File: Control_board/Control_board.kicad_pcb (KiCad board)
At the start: 4 copper layers, 123.8 x 99.7 mm, 26 parts, among them J1 ICSP, J2 Conn_02x32_Odd_Even, J3 Conn_02x32_Odd_Even, SW1 SW_Push, SW2 SW_Push, U1 74LS74, U10 27C512, U11 ATtiny85-20P, U2 74LS74, U3 74LS273, U4 74LS373, U5 74LS192, U6 74LS373, U7 27C512, U8 27C512, U9 27C512

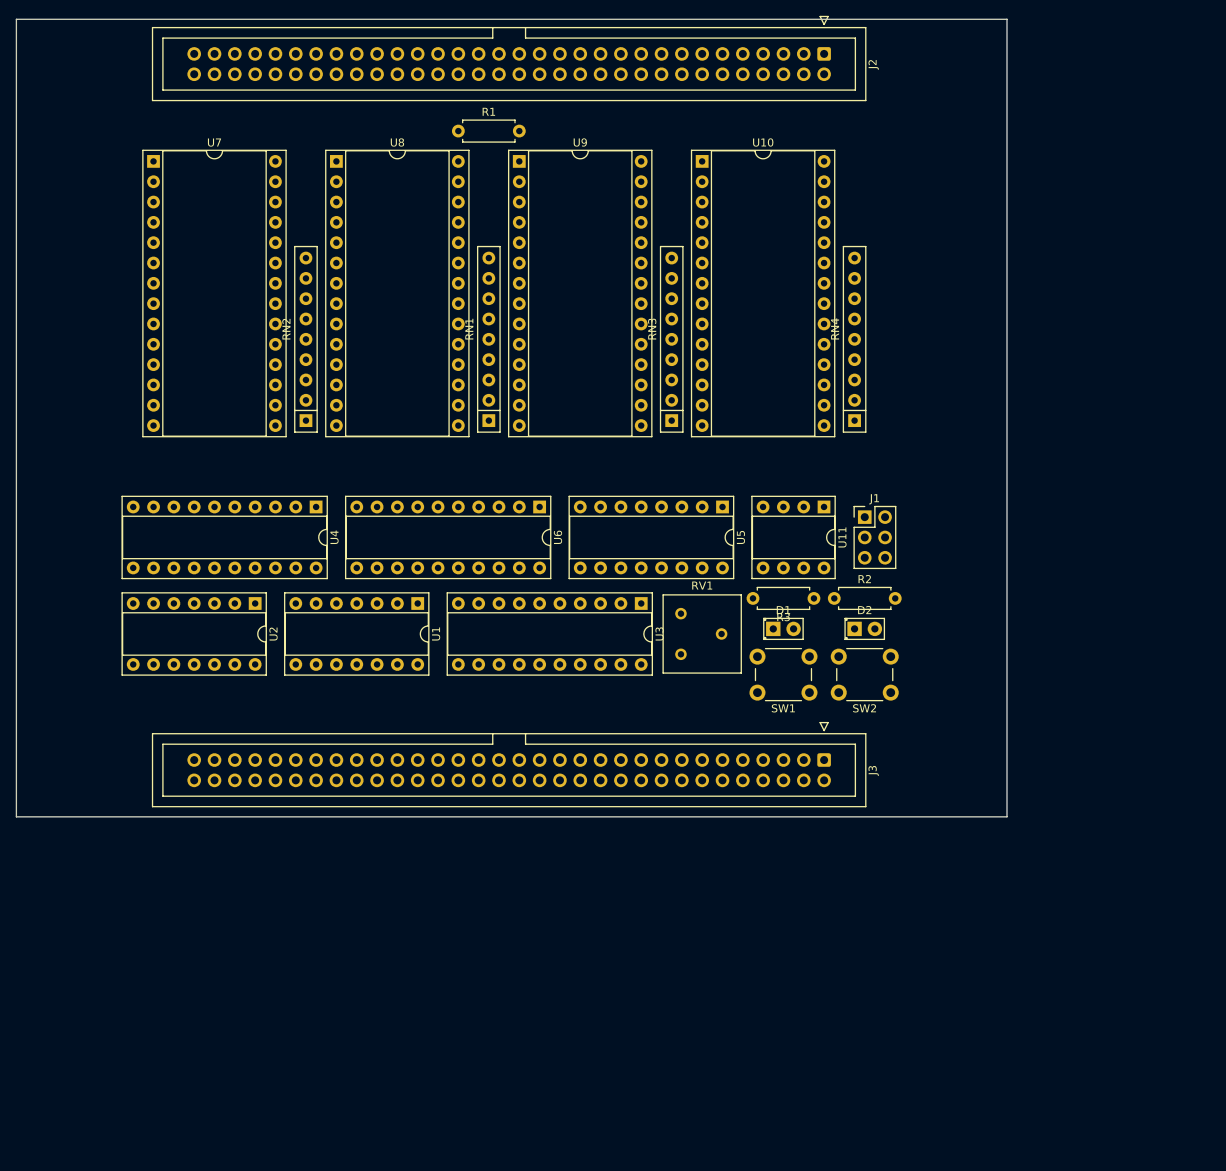
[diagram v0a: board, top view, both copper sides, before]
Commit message: Control board ready for routing
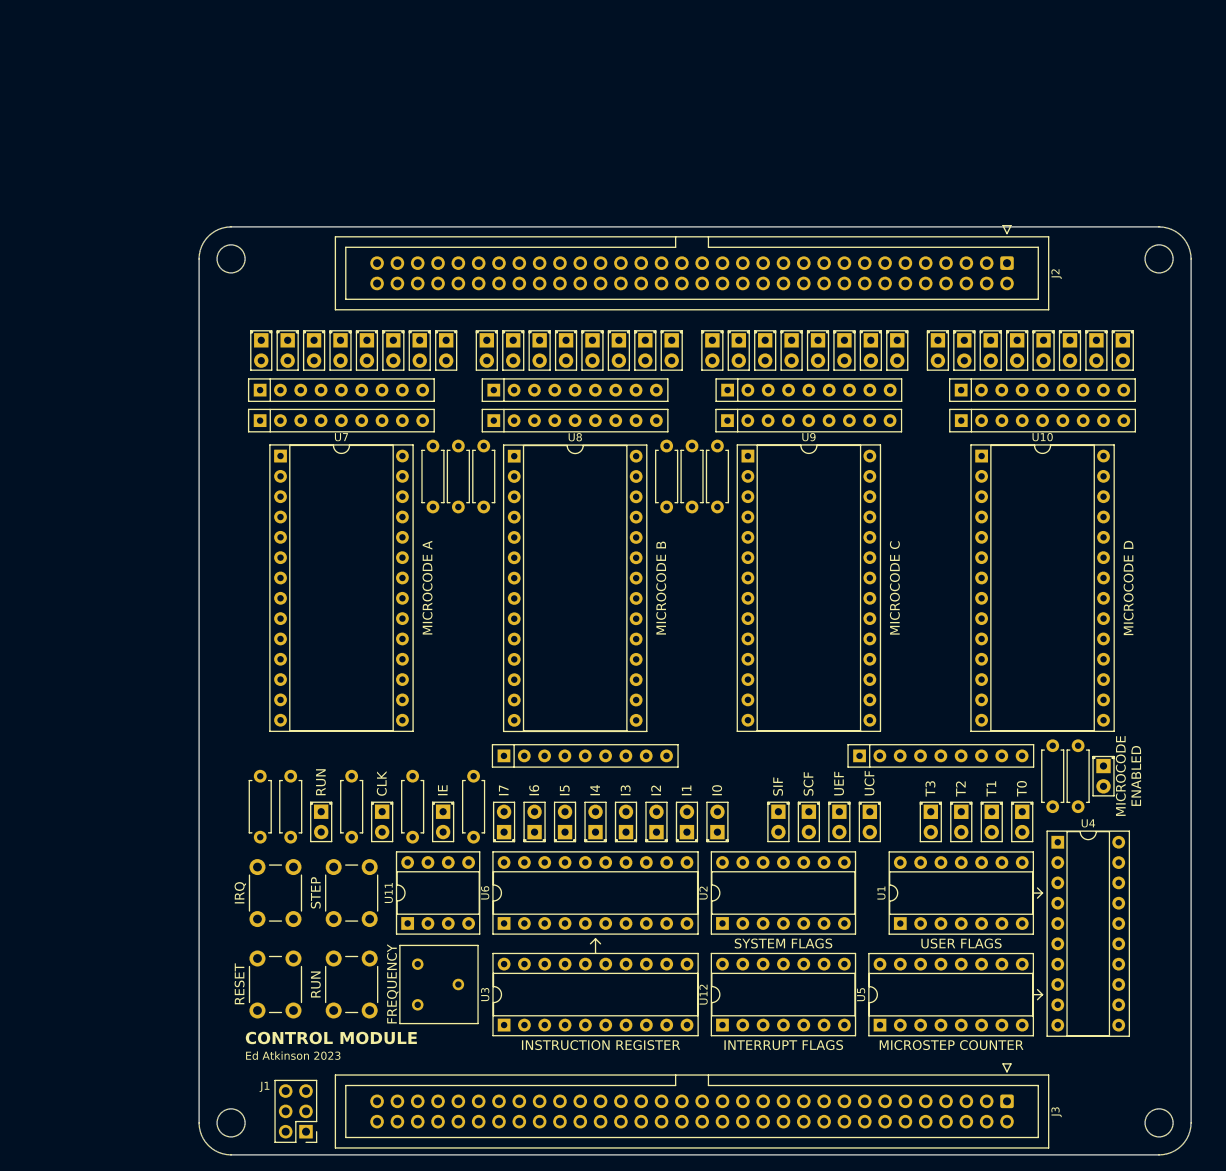
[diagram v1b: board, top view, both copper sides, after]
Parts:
- added D10: LED, LED_THT:LED_D2.0mm_W4.8mm_H2.5mm_FlatTop, F.Cu at (149.2, 118.1)
- added D11: LED, LED_THT:LED_D2.0mm_W4.8mm_H2.5mm_FlatTop, F.Cu at (145.4, 118.1)
- added D12: LED, LED_THT:LED_D2.0mm_W4.8mm_H2.5mm_FlatTop, F.Cu at (137.8, 120.7)
- added D13: LED, LED_THT:LED_D2.0mm_W4.8mm_H2.5mm_FlatTop, F.Cu at (134.0, 120.7)
- added D14: LED, LED_THT:LED_D2.0mm_W4.8mm_H2.5mm_FlatTop, F.Cu at (130.2, 120.7)
- added D15: LED, LED_THT:LED_D2.0mm_W4.8mm_H2.5mm_FlatTop, F.Cu at (126.4, 120.7)
- added D16: LED, LED_THT:LED_D2.0mm_W4.8mm_H2.5mm_FlatTop, F.Cu at (122.6, 120.7)
- added D17: LED, LED_THT:LED_D2.0mm_W4.8mm_H2.5mm_FlatTop, F.Cu at (118.7, 120.7)
- added D18: LED, LED_THT:LED_D2.0mm_W4.8mm_H2.5mm_FlatTop, F.Cu at (114.9, 120.7)
- added D19: LED, LED_THT:LED_D2.0mm_W4.8mm_H2.5mm_FlatTop, F.Cu at (111.1, 120.7)
- added D20: LED, LED_THT:LED_D2.0mm_W4.8mm_H2.5mm_FlatTop, F.Cu at (125.5, 59.2)
- added D21: LED, LED_THT:LED_D2.0mm_W4.8mm_H2.5mm_FlatTop, F.Cu at (122.2, 59.2)
- added D22: LED, LED_THT:LED_D2.0mm_W4.8mm_H2.5mm_FlatTop, F.Cu at (115.6, 59.2)
- added D23: LED, LED_THT:LED_D2.0mm_W4.8mm_H2.5mm_FlatTop, F.Cu at (109.0, 59.2)
- added D24: LED, LED_THT:LED_D2.0mm_W4.8mm_H2.5mm_FlatTop, F.Cu at (112.3, 59.2)
- added D25: LED, LED_THT:LED_D2.0mm_W4.8mm_H2.5mm_FlatTop, F.Cu at (118.9, 59.2)
- added D26: LED, LED_THT:LED_D2.0mm_W4.8mm_H2.5mm_FlatTop, F.Cu at (128.8, 59.2)
- added D27: LED, LED_THT:LED_D2.0mm_W4.8mm_H2.5mm_FlatTop, F.Cu at (132.1, 59.2)
- added D28: LED, LED_THT:LED_D2.0mm_W4.8mm_H2.5mm_FlatTop, F.Cu at (80.8, 59.2)
- added D29: LED, LED_THT:LED_D2.0mm_W4.8mm_H2.5mm_FlatTop, F.Cu at (84.1, 59.2)
- added D3: LED, LED_THT:LED_D2.0mm_W4.8mm_H2.5mm_FlatTop, F.Cu at (175.9, 118.1)
- added D30: LED, LED_THT:LED_D2.0mm_W4.8mm_H2.5mm_FlatTop, F.Cu at (87.4, 59.2)
- added D31: LED, LED_THT:LED_D2.0mm_W4.8mm_H2.5mm_FlatTop, F.Cu at (90.7, 59.2)
- added D32: LED, LED_THT:LED_D2.0mm_W4.8mm_H2.5mm_FlatTop, F.Cu at (94.0, 59.2)
- added D33: LED, LED_THT:LED_D2.0mm_W4.8mm_H2.5mm_FlatTop, F.Cu at (97.3, 59.2)
- added D34: LED, LED_THT:LED_D2.0mm_W4.8mm_H2.5mm_FlatTop, F.Cu at (100.6, 59.2)
- added D35: LED, LED_THT:LED_D2.0mm_W4.8mm_H2.5mm_FlatTop, F.Cu at (103.9, 59.2)
- added D36: LED, LED_THT:LED_D2.0mm_W4.8mm_H2.5mm_FlatTop, F.Cu at (160.3, 59.2)
- added D37: LED, LED_THT:LED_D2.0mm_W4.8mm_H2.5mm_FlatTop, F.Cu at (157.0, 59.2)
- added D38: LED, LED_THT:LED_D2.0mm_W4.8mm_H2.5mm_FlatTop, F.Cu at (153.7, 59.2)
- added D39: LED, LED_THT:LED_D2.0mm_W4.8mm_H2.5mm_FlatTop, F.Cu at (150.4, 59.2)
- added D4: LED, LED_THT:LED_D2.0mm_W4.8mm_H2.5mm_FlatTop, F.Cu at (172.1, 118.1)
- added D40: LED, LED_THT:LED_D2.0mm_W4.8mm_H2.5mm_FlatTop, F.Cu at (147.1, 59.2)
- added D41: LED, LED_THT:LED_D2.0mm_W4.8mm_H2.5mm_FlatTop, F.Cu at (143.8, 59.2)
- added D42: LED, LED_THT:LED_D2.0mm_W4.8mm_H2.5mm_FlatTop, F.Cu at (140.5, 59.2)
- added D43: LED, LED_THT:LED_D2.0mm_W4.8mm_H2.5mm_FlatTop, F.Cu at (137.2, 59.2)
- added D44: LED, LED_THT:LED_D2.0mm_W4.8mm_H2.5mm_FlatTop, F.Cu at (165.4, 59.2)
- added D45: LED, LED_THT:LED_D2.0mm_W4.8mm_H2.5mm_FlatTop, F.Cu at (185.2, 59.2)
- added D46: LED, LED_THT:LED_D2.0mm_W4.8mm_H2.5mm_FlatTop, F.Cu at (181.9, 59.2)
- added D47: LED, LED_THT:LED_D2.0mm_W4.8mm_H2.5mm_FlatTop, F.Cu at (178.6, 59.2)
- added D48: LED, LED_THT:LED_D2.0mm_W4.8mm_H2.5mm_FlatTop, F.Cu at (175.3, 59.2)
- added D49: LED, LED_THT:LED_D2.0mm_W4.8mm_H2.5mm_FlatTop, F.Cu at (172.0, 59.2)
- added D5: LED, LED_THT:LED_D2.0mm_W4.8mm_H2.5mm_FlatTop, F.Cu at (168.3, 118.1)
- added D50: LED, LED_THT:LED_D2.0mm_W4.8mm_H2.5mm_FlatTop, F.Cu at (168.7, 59.2)
- added D51: LED, LED_THT:LED_D2.0mm_W4.8mm_H2.5mm_FlatTop, F.Cu at (188.5, 59.2)
- added D52: LED, LED_THT:LED_D2.0mm_W4.8mm_H2.5mm_FlatTop, F.Cu at (186.1, 112.4)
- added D6: LED, LED_THT:LED_D2.0mm_W4.8mm_H2.5mm_FlatTop, F.Cu at (103.5, 118.1)
- added D7: LED, LED_THT:LED_D2.0mm_W4.8mm_H2.5mm_FlatTop, F.Cu at (164.5, 118.1)
- added D8: LED, LED_THT:LED_D2.0mm_W4.8mm_H2.5mm_FlatTop, F.Cu at (156.8, 118.1)
- added D9: LED, LED_THT:LED_D2.0mm_W4.8mm_H2.5mm_FlatTop, F.Cu at (153.0, 118.1)
- added H1: MountingHole, MountingHole:MountingHole_3.5mm, F.Cu at (77.0, 49.0)
- added H2: MountingHole, MountingHole:MountingHole_3.5mm, F.Cu at (193.0, 49.0)
- added H3: MountingHole, MountingHole:MountingHole_3.5mm, F.Cu at (77.0, 157.0)
- added H4: MountingHole, MountingHole:MountingHole_3.5mm, F.Cu at (193.0, 157.0)
- added R10: 1K, Resistor_THT:R_Axial_DIN0207_L6.3mm_D2.5mm_P7.62mm_Horizontal, F.Cu at (80.6, 113.7)
- added R11: 1K, Resistor_THT:R_Axial_DIN0207_L6.3mm_D2.5mm_P7.62mm_Horizontal, F.Cu at (179.7, 109.9)
- added R12: 330R, Resistor_THT:R_Axial_DIN0207_L6.3mm_D2.5mm_P7.62mm_Horizontal, F.Cu at (182.9, 109.9)
- added R13: 1K, Resistor_THT:R_Axial_DIN0207_L6.3mm_D2.5mm_P7.62mm_Horizontal, F.Cu at (84.5, 113.7)
- added R4: 330R, Resistor_THT:R_Axial_DIN0207_L6.3mm_D2.5mm_P7.62mm_Horizontal, F.Cu at (107.3, 113.7)
- added R5: 1K, Resistor_THT:R_Axial_DIN0207_L6.3mm_D2.5mm_P7.62mm_Horizontal, F.Cu at (137.8, 80.0)
- added R6: 1K, Resistor_THT:R_Axial_DIN0207_L6.3mm_D2.5mm_P7.62mm_Horizontal, F.Cu at (134.6, 80.0)
- added R7: 330R, Resistor_THT:R_Axial_DIN0207_L6.3mm_D2.5mm_P7.62mm_Horizontal, F.Cu at (108.6, 80.0)
- added R8: 330R, Resistor_THT:R_Axial_DIN0207_L6.3mm_D2.5mm_P7.62mm_Horizontal, F.Cu at (105.4, 80.0)
- added R9: 330R, Resistor_THT:R_Axial_DIN0207_L6.3mm_D2.5mm_P7.62mm_Horizontal, F.Cu at (102.2, 80.0)
- added RN10: 330R, Resistor_THT:R_Array_SIP9, F.Cu at (168.3, 65.4)
- added RN5: 330R, Resistor_THT:R_Array_SIP9, F.Cu at (155.6, 111.1)
- added RN6: 330R, Resistor_THT:R_Array_SIP9, F.Cu at (111.1, 111.1)
- added RN7: 330R, Resistor_THT:R_Array_SIP9, F.Cu at (109.8, 65.4)
- added RN8: 330R, Resistor_THT:R_Array_SIP9, F.Cu at (80.6, 65.4)
- added RN9: 330R, Resistor_THT:R_Array_SIP9, F.Cu at (139.1, 65.4)
- added SW3: SW_Push, Button_Switch_THT:SW_PUSH_6mm, F.Cu at (80.3, 142.9)
- added SW4: SW_Push, Button_Switch_THT:SW_PUSH_6mm, F.Cu at (80.3, 131.5)
- added U12: 74LS74, Package_DIP:DIP-14_W7.62mm_Socket, F.Cu at (138.4, 144.8)
- RN1, RN2, RN3, RN4: value R_Network08 -> 1K
- moved J1 103.8 mm to (86.4, 158.1), turned to 180 degrees
- moved U4 101.7 mm to (180.3, 121.9), turned to 0 degrees
- moved U11 73.6 mm to (99.1, 132.1), turned to 90 degrees
- moved U1 72.4 mm to (160.7, 132.1), turned to 90 degrees
- moved U2 70.8 mm to (138.4, 132.1), turned to 90 degrees
- moved SW2 68.7 mm to (94.3, 125.0), turned to -90 degrees
- moved U5 67.7 mm to (158.1, 144.8), turned to 90 degrees
- moved R2 64.3 mm to (92.1, 113.7), turned to -90 degrees
- moved SW1 64.2 mm to (94.3, 136.4), turned to -90 degrees
- moved D2 63.3 mm to (95.9, 118.1), turned to -90 degrees
- moved D1 61.0 mm to (88.3, 118.1), turned to -90 degrees
- moved U3 55.4 mm to (111.1, 144.8), turned to 90 degrees
- moved R3 54.9 mm to (99.7, 113.7), turned to -90 degrees
- moved RV1 54.8 mm to (100.3, 142.2)
- moved R1 53.7 mm to (131.4, 80.0), turned to 90 degrees
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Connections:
- J2 pad 13: /INTERRUPT_FLAG -> /~{INTERRUPT_FLAG}
- J3 pad 13: /INTERRUPT_FLAG -> /~{INTERRUPT_FLAG}
- RN1 pad 5: unconnected-(RN1-R4-Pad5) -> /COUNTER_RESET
- RN1 pad 6: /COUNTER_RESET -> unconnected-(RN1-R5-Pad6)
- RN1 pad 7: /INTERRUPT_UPDATE -> unconnected-(RN1-R6-Pad7)
- U1 pad 1: unconnected-(U1A-~{R}-Pad1) -> +5V
- U1 pad 10: unconnected-(U1B-~{S}-Pad10) -> +5V
- U1 pad 13: unconnected-(U1B-~{R}-Pad13) -> +5V
- U1 pad 4: unconnected-(U1A-~{S}-Pad4) -> +5V
- U2 pad 1: unconnected-(U2A-~{R}-Pad1) -> +5V
- U2 pad 10: unconnected-(U2B-~{S}-Pad10) -> +5V
- U2 pad 11: /INTERRUPT_UPDATE -> GND
- U2 pad 12: /INTERRUPT_FLAG -> GND
- U2 pad 13: /~{RESET} -> +5V
- U2 pad 4: unconnected-(U2A-~{S}-Pad4) -> +5V
- U2 pad 9: Net-(U2B-Q) -> unconnected-(U2B-Q-Pad9)
- U4 pad 12: unconnected-(U4-O4-Pad12) -> /MA4
- U4 pad 13: GND -> Net-(U1A-Q)
- U4 pad 14: GND -> Net-(U1B-Q)
- U4 pad 15: unconnected-(U4-O5-Pad15) -> /MA5
- U4 pad 16: unconnected-(U4-O6-Pad16) -> /MA6
- U4 pad 17: GND -> Net-(U2A-Q)
- U4 pad 18: GND -> Net-(U12A-Q)
- U4 pad 19: unconnected-(U4-O7-Pad19) -> /MA7
- U4 pad 2: /MA12 -> /MA0
- U4 pad 3: Net-(U1A-Q) -> Net-(U4-D0)
- U4 pad 4: Net-(U1B-Q) -> Net-(U4-D1)
- U4 pad 5: /MA13 -> /MA1
- U4 pad 6: /MA14 -> /MA2
- U4 pad 7: Net-(U2A-Q) -> Net-(U4-D2)
- U4 pad 8: Net-(U2B-Q) -> Net-(U4-D3)
- U4 pad 9: /MA15 -> /MA3
- U5 pad 2: /MA1 -> Net-(U4-D1)
- U5 pad 3: /MA0 -> Net-(U4-D0)
- U5 pad 6: /MA2 -> Net-(U4-D2)
- U5 pad 7: /MA3 -> Net-(U4-D3)
- U6 pad 12: /MA8 -> /MA12
- U6 pad 15: /MA9 -> /MA13
- U6 pad 16: /MA10 -> /MA14
- U6 pad 19: /MA11 -> /MA15
- U6 pad 2: /MA4 -> /MA8
- U6 pad 5: /MA5 -> /MA9
- U6 pad 6: /MA6 -> /MA10
- U6 pad 9: /MA7 -> /MA11
- U8 pad 15: unconnected-(U8-D3-Pad15) -> /COUNTER_RESET
- U8 pad 16: /COUNTER_RESET -> /~{INTERRUPT_ENABLE}
- U8 pad 17: /INTERRUPT_UPDATE -> /~{INTERRUPT_DISABLE}
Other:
- board size 123.8 x 99.7 mm -> 124 x 116 mm
- board text added: "CLK"
- board text added: "CONTROL MODULE"
- board text added: "Ed Atkinson 2023"
- board text added: "FREQUENCY"
- board text added: "I0"
- board text added: "I1"
- board text added: "I2"
- board text added: "I3"
- board text added: "I4"
- board text added: "I5"
- board text added: "I6"
- board text added: "I7"
- board text added: "IE"
- board text added: "INSTRUCTION REGISTER"
- board text added: "INTERRUPT FLAGS"
- board text added: "IRQ"
- board text added: "MICROCODE A"
- board text added: "MICROCODE B"
- board text added: "MICROCODE C"
- board text added: "MICROCODE D"
- board text added: "MICROCODE ENABLED"
- board text added: "MICROSTEP COUNTER"
- board text added: "RESET"
- board text added: "RUN"
- board text added: "SCF"
- board text added: "SIF"
- board text added: "STEP"
- board text added: "SYSTEM FLAGS"
- board text added: "T0"
- board text added: "T1"
- board text added: "T2"
- board text added: "T3"
- board text added: "UCF"
- board text added: "UEF"
- board text added: "USER FLAGS"

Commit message: Control board and connector bridge ready for ordering
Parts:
- J3: value Conn_02x32_Odd_Even -> Conn_01x02; footprint Connector_IDC:IDC-Header_2x32_P2.54mm_Vertical -> Connector_PinHeader_2.54mm:PinHeader_1x02_P2.54mm_Vertical
- moved R9 63.5 mm to (163.8, 64.8), turned to -90 degrees
- moved R6 59.7 mm to (194.3, 82.5)
- moved R1 59.1 mm to (190.5, 82.5)
- moved RN7 58.4 mm to (168.3, 65.4)
- moved RN1 58.4 mm to (168.3, 69.2)
- moved RN3 58.4 mm to (80.6, 69.2)
- moved R7 57.4 mm to (165.7, 74.9), turned to -90 degrees
- moved R8 56.7 mm to (161.9, 74.9), turned to -90 degrees
- moved D23 56.4 mm to (165.4, 59.2)
- moved D20 56.4 mm to (181.9, 59.2)
- moved D21 56.4 mm to (178.6, 59.2)
- moved D22 56.4 mm to (172.0, 59.2)
- moved D24 56.4 mm to (168.7, 59.2)
- moved D26 56.4 mm to (185.2, 59.2)
- moved D25 56.4 mm to (175.3, 59.2)
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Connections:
- D20 pad 1: /~{INTERRUPT_DISABLE} -> /IR_LOAD
- D21 pad 1: /~{INTERRUPT_ENABLE} -> /INT_EN_TOGGLE
- D28 pad 1: Net-(D28-K) -> /~{SP_OUT}
- D28 pad 2: /PC_H_LOAD -> Net-(D28-A)
- D29 pad 1: Net-(D29-K) -> /~{ALU_OUT}
- D29 pad 2: /PC_L_LOAD -> Net-(D29-A)
- D30 pad 1: Net-(D30-K) -> /~{PC_OUT}
- D30 pad 2: /SP_H_LOAD -> Net-(D30-A)
- D31 pad 1: Net-(D31-K) -> /~{A_OUT}
- D31 pad 2: /SP_L_LOAD -> Net-(D31-A)
- D32 pad 1: Net-(D32-K) -> /~{T_OUT}
- D32 pad 2: /B_LOAD -> Net-(D32-A)
- D33 pad 1: Net-(D33-K) -> /~{BC_OUT}
- D33 pad 2: /C_LOAD -> Net-(D33-A)
- D34 pad 1: Net-(D34-K) -> /~{DE_OUT}
- D34 pad 2: /D_LOAD -> Net-(D34-A)
- D35 pad 1: Net-(D35-K) -> /~{RAM_OUT}
- D35 pad 2: /E_LOAD -> Net-(D35-A)
- D36 pad 1: /~{PC_OUT} -> Net-(D36-K)
- D36 pad 2: Net-(D36-A) -> /PC_H_LOAD
- D37 pad 1: /~{SP_OUT} -> Net-(D37-K)
- D37 pad 2: Net-(D37-A) -> /SP_H_LOAD
- D38 pad 1: /~{BC_OUT} -> Net-(D38-K)
- D38 pad 2: Net-(D38-A) -> /B_LOAD
- D39 pad 1: /~{DE_OUT} -> Net-(D39-K)
- D39 pad 2: Net-(D39-A) -> /PC_L_LOAD
- D40 pad 1: /~{A_OUT} -> Net-(D40-K)
- D40 pad 2: Net-(D40-A) -> /C_LOAD
- D41 pad 1: /~{T_OUT} -> Net-(D41-K)
- D41 pad 2: Net-(D41-A) -> /SP_L_LOAD
- D42 pad 1: /~{ALU_OUT} -> Net-(D42-K)
- D42 pad 2: Net-(D42-A) -> /E_LOAD
- D43 pad 1: /~{RAM_OUT} -> Net-(D43-K)
- D43 pad 2: Net-(D43-A) -> /D_LOAD
- D44 pad 1: /~{ADR_L_OUT} -> /~{ADR_H_OUT}
- D45 pad 1: /~{ADR_H_OUT} -> /ALU_M
- D46 pad 1: /ALU_M -> /~{ADR_L_OUT}
- D47 pad 1: /ALU_S0 -> /~{ALU_CIN}
- D48 pad 1: /ALU_S1 -> /ALU_S0
- D49 pad 1: /ALU_S2 -> /ALU_S1
- D50 pad 1: /ALU_S3 -> /ALU_S2
- D51 pad 1: /~{ALU_CIN} -> /ALU_S3
- R1 pad 2: /~{RAM_LOAD} -> /IR_LOAD
- R5 pad 2: /~{INTERRUPT_DISABLE} -> /INT_EN_TOGGLE
- R6 pad 2: /~{INTERRUPT_ENABLE} -> /~{RAM_LOAD}
- RN10 pad 2: Net-(D51-A) -> Net-(D44-A)
- RN10 pad 3: Net-(D50-A) -> Net-(D45-A)
- RN10 pad 4: Net-(D49-A) -> Net-(D46-A)
- RN10 pad 5: Net-(D48-A) -> Net-(D47-A)
- RN10 pad 6: Net-(D47-A) -> Net-(D48-A)
- RN10 pad 7: Net-(D46-A) -> Net-(D49-A)
- RN10 pad 8: Net-(D45-A) -> Net-(D50-A)
- RN10 pad 9: Net-(D44-A) -> Net-(D51-A)
- RN2 pad 3: /PC_L_LOAD -> /SP_H_LOAD
- RN2 pad 4: /SP_H_LOAD -> /B_LOAD
- RN2 pad 5: /SP_L_LOAD -> /PC_L_LOAD
- RN2 pad 6: /B_LOAD -> /C_LOAD
- RN2 pad 7: /C_LOAD -> /SP_L_LOAD
- RN2 pad 8: /D_LOAD -> /E_LOAD
- RN2 pad 9: /E_LOAD -> /D_LOAD
- RN3 pad 2: /~{RAM_OUT} -> /~{SP_OUT}
- RN3 pad 4: /~{T_OUT} -> /~{PC_OUT}
- RN3 pad 6: /~{DE_OUT} -> /~{T_OUT}
- RN3 pad 8: /~{SP_OUT} -> /~{DE_OUT}
- RN3 pad 9: /~{PC_OUT} -> /~{RAM_OUT}
- RN4 pad 2: /~{ALU_CIN} -> /~{ADR_H_OUT}
- RN4 pad 3: /ALU_S3 -> /ALU_M
- RN4 pad 4: /ALU_S2 -> /~{ADR_L_OUT}
- RN4 pad 5: /ALU_S1 -> /~{ALU_CIN}
- RN4 pad 7: /ALU_M -> /ALU_S1
- RN4 pad 8: /~{ADR_H_OUT} -> /ALU_S2
- RN4 pad 9: /~{ADR_L_OUT} -> /ALU_S3
- RN8 pad 1: GND -> +5V
- RN8 pad 2: Net-(D28-K) -> Net-(D28-A)
- RN8 pad 3: Net-(D29-K) -> Net-(D29-A)
- RN8 pad 4: Net-(D30-K) -> Net-(D30-A)
- RN8 pad 5: Net-(D31-K) -> Net-(D31-A)
- RN8 pad 6: Net-(D32-K) -> Net-(D32-A)
- RN8 pad 7: Net-(D33-K) -> Net-(D33-A)
- RN8 pad 8: Net-(D34-K) -> Net-(D34-A)
- RN8 pad 9: Net-(D35-K) -> Net-(D35-A)
- RN9 pad 1: +5V -> GND
- RN9 pad 2: Net-(D43-A) -> Net-(D36-K)
- RN9 pad 3: Net-(D42-A) -> Net-(D37-K)
- RN9 pad 4: Net-(D41-A) -> Net-(D38-K)
- RN9 pad 5: Net-(D40-A) -> Net-(D39-K)
- RN9 pad 6: Net-(D39-A) -> Net-(D40-K)
- RN9 pad 7: Net-(D38-A) -> Net-(D41-K)
- RN9 pad 8: Net-(D37-A) -> Net-(D42-K)
- RN9 pad 9: Net-(D36-A) -> Net-(D43-K)
- U10 pad 11: /~{ADR_L_OUT} -> /A_LOAD
- U10 pad 12: /~{ADR_H_OUT} -> /T_LOAD
- U10 pad 13: /ALU_M -> /~{RAM_LOAD}
- U10 pad 15: /ALU_S0 -> /COUNTER_RESET
- U10 pad 16: /ALU_S1 -> /INT_EN_TOGGLE
- U10 pad 17: /ALU_S2 -> /IR_LOAD
- U10 pad 18: /ALU_S3 -> /FLAGS_A_UPDATE
- U10 pad 19: /~{ALU_CIN} -> /FLAGS_B_UPDATE
- U10 pad 22: GND -> /CLK
- U12 pad 10: /~{INTERRUPT_DISABLE} -> +5V
- U12 pad 11: GND -> /INT_EN_TOGGLE
- U12 pad 12: GND -> Net-(U12B-D)
- U12 pad 13: /~{INTERRUPT_ENABLE} -> /~{RESET}
- U12 pad 8: unconnected-(U12B-~{Q}-Pad8) -> Net-(U12B-D)
- U7 pad 11: /PC_H_LOAD -> /~{SP_OUT}
- U7 pad 12: /PC_L_LOAD -> /~{ALU_OUT}
- U7 pad 13: /SP_H_LOAD -> /~{PC_OUT}
- U7 pad 15: /SP_L_LOAD -> /~{A_OUT}
- U7 pad 16: /B_LOAD -> /~{T_OUT}
- U7 pad 17: /C_LOAD -> /~{BC_OUT}
- U7 pad 18: /D_LOAD -> /~{DE_OUT}
- U7 pad 19: /E_LOAD -> /~{RAM_OUT}
- U7 pad 22: /CLK -> GND
- U8 pad 11: /A_LOAD -> /PC_H_LOAD
- U8 pad 12: /T_LOAD -> /SP_H_LOAD
- U8 pad 13: /~{RAM_LOAD} -> /B_LOAD
- U8 pad 15: /COUNTER_RESET -> /PC_L_LOAD
- U8 pad 16: /~{INTERRUPT_ENABLE} -> /C_LOAD
- U8 pad 17: /~{INTERRUPT_DISABLE} -> /SP_L_LOAD
- U8 pad 18: /FLAGS_A_UPDATE -> /E_LOAD
- U8 pad 19: /FLAGS_B_UPDATE -> /D_LOAD
- U9 pad 11: /~{PC_OUT} -> /~{ADR_H_OUT}
- U9 pad 12: /~{SP_OUT} -> /ALU_M
- U9 pad 13: /~{BC_OUT} -> /~{ADR_L_OUT}
- U9 pad 15: /~{DE_OUT} -> /~{ALU_CIN}
- U9 pad 16: /~{A_OUT} -> /ALU_S0
- U9 pad 17: /~{T_OUT} -> /ALU_S1
- U9 pad 18: /~{ALU_OUT} -> /ALU_S2
- U9 pad 19: /~{RAM_OUT} -> /ALU_S3
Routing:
- net +5V: track 0.00 -> 684.8 mm, vias 0 -> 6
- net /CLK: track 0.00 -> 355.3 mm
- net /D3: track 0.00 -> 257.5 mm, vias 0 -> 1
- net /D2: track 0.00 -> 248.8 mm, vias 0 -> 1
- net /D1: track 0.00 -> 243.7 mm
- net /CONTROL_DISABLE: track 0.00 -> 239.0 mm
- net /D0: track 0.00 -> 234.7 mm
- net /~{INTERRUPT_FLAG}: track 0.00 -> 230.4 mm, vias 0 -> 3
- net /~{RESET}: track 0.00 -> 217.2 mm, vias 0 -> 1
- net /D6: track 0.00 -> 209.7 mm, vias 0 -> 1
- net /D7: track 0.00 -> 207.0 mm, vias 0 -> 1
- net /D4: track 0.00 -> 203.2 mm, vias 0 -> 2
- net /D5: track 0.00 -> 201.9 mm, vias 0 -> 2
- net /MA4: track 0.00 -> 193.0 mm, vias 0 -> 1
- net /MA6: track 0.00 -> 189.4 mm, vias 0 -> 1
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- added copper zone on B.Cu, net GND
- added copper zone on F.Cu, net GND
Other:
- board size 124 x 116 mm -> 124 x 113 mm
- copper layers 4 -> 2
- board text added: "ABHo"
- board text added: "ABLo"
- board text added: "Ai"
- board text added: "Ao"
- board text added: "BCo"
- board text added: "Bi"
- board text added: "CLOCK GENERATOR"
- board text added: "Ci"
- board text added: "DEo"
- board text added: "Di"
- board text added: "Ei"
- board text added: "FSi"
- board text added: "FUi"
- board text added: "HIGH LATCH"
- board text added: "IEi"
- board text added: "INTERRUPT"
- board text added: "IRi"
- board text added: "JLCJLCJLCJLC"
- board text added: "LOW LATCH"
- board text added: "Lc"
- board text added: "Lm"
- board text added: "Lo"
- board text added: "Ls0"
- board text added: "Ls1"
- board text added: "Ls2"
- board text added: "Ls3"
- board text added: "MAr"
- board text added: "Mi"
- board text added: "Mo"
- board text added: "PCHi"
- board text added: "PCLi"
- board text added: "PCo"
- board text added: "SPHi"
- board text added: "SPLi"
- board text added: "SPo"
- board text added: "Ti"
- board text added: "To"
- board text removed: "IRQ"

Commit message: Memory board
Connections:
- U5 pad 4: GND -> +5V
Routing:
- net +5V: track 684.8 -> 708.1 mm
- net GND: vias 175 -> 174
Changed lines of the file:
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@@
       (net 153 "Net-(U4-D0)") (pinfunction "QA") (pintype "output"))
     (pad "4" thru_hole oval (at 0 7.62 90) (size 1.6 1.6) (drill 0.8) (layers "*.Cu" "*.Mask")
-      (net 9 "GND") (pinfunction "DOWN") (pintype "input"))
+      (net 5 "+5V") (pinfunction "DOWN") (pintype "input"))
     (pad "5" thru_hole oval (at 0 10.16 90) (size 1.6 1.6) (drill 0.8) (layers "*.Cu" "*.Mask")
       (net 4 "/CLK") (pinfunction "UP") (pintype "input"))
@@
   (segment (start 158.745 126.37) (end 160.655 124.46) (width 0.5) (layer "B.Cu") (net 5))
   (segment (start 191.135 123.19) (end 189.865 121.92) (width 0.5) (layer "B.Cu") (net 5))
+  (segment (start 165.735 146.05) (end 164.465 147.32) (width 0.5) (layer "B.Cu") (net 5))
   (segment (start 175.895 73.66) (end 186.055 73.66) (width 0.5) (layer "B.Cu") (net 5))
   (segment (start 138.425 139.06) (end 138.43 139.065) (width 0.5) (layer "B.Cu") (net 5))
@@
   (segment (start 140.965 124.45) (end 138.425 124.45) (width 0.5) (layer "B.Cu") (net 5))
   (segment (start 189.865 121.92) (end 187.955 121.92) (width 0.5) (layer "B.Cu") (net 5))
+  (segment (start 147.32 147.32) (end 146.045 146.045) (width 0.5) (layer "B.Cu") (net 5))
+  (segment (start 146.045 146.045) (end 146.045 144.77) (width 0.5) (layer "B.Cu") (net 5))
+  (segment (start 165.735 144.78) (end 165.735 146.05) (width 0.5) (layer "B.Cu") (net 5))
   (segment (start 190.5 71.755) (end 190.5 72.39) (width 0.5) (layer "B.Cu") (net 5))
+  (segment (start 164.465 147.32) (end 147.32 147.32) (width 0.5) (layer "B.Cu") (net 5))
   (segment (start 170.815 124.46) (end 174.625 128.27) (width 0.5) (layer "B.Cu") (net 5))
   (segment (start 138.425 132.07) (end 138.425 124.45) (width 0.5) (layer "B.Cu") (net 5))
@@
   (via (at 154.305 113.03) (size 0.8) (drill 0.4) (layers "F.Cu" "B.Cu") (free) (net 9))
   (via (at 94.615 146.05) (size 0.8) (drill 0.4) (layers "F.Cu" "B.Cu") (free) (net 9))
-  (via (at 147.955 146.685) (size 0.8) (drill 0.4) (layers "F.Cu" "B.Cu") (free) (net 9))
   (via (at 73.66 65.405) (size 0.8) (drill 0.4) (layers "F.Cu" "B.Cu") (free) (net 9))
   (via (at 118.11 108.585) (size 0.8) (drill 0.4) (layers "F.Cu" "B.Cu") (free) (net 9))
